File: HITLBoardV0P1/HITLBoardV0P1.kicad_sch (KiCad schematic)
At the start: 4 parts, among them SW1 SW_Push

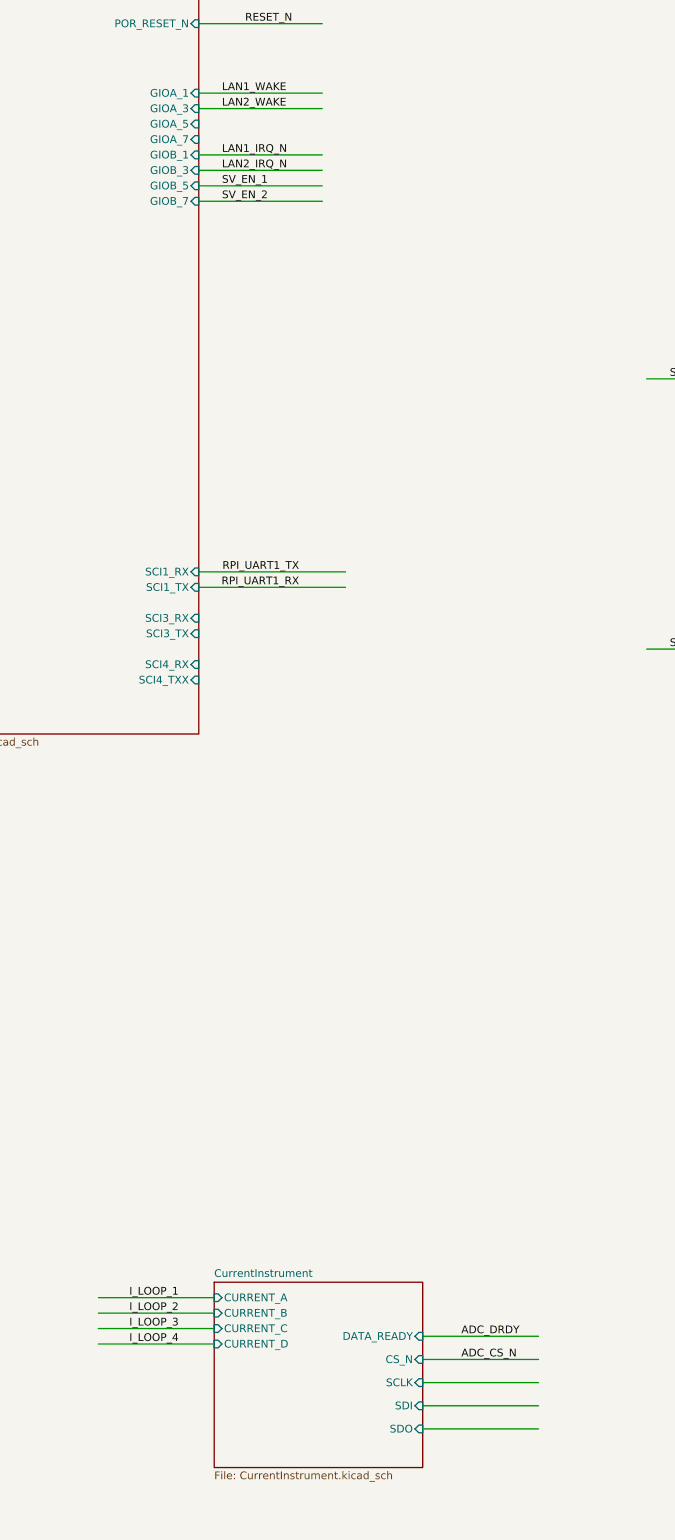
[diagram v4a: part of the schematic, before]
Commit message: FIX spi 3 on tmdx for current loop ADC, add gpio pin for data ready
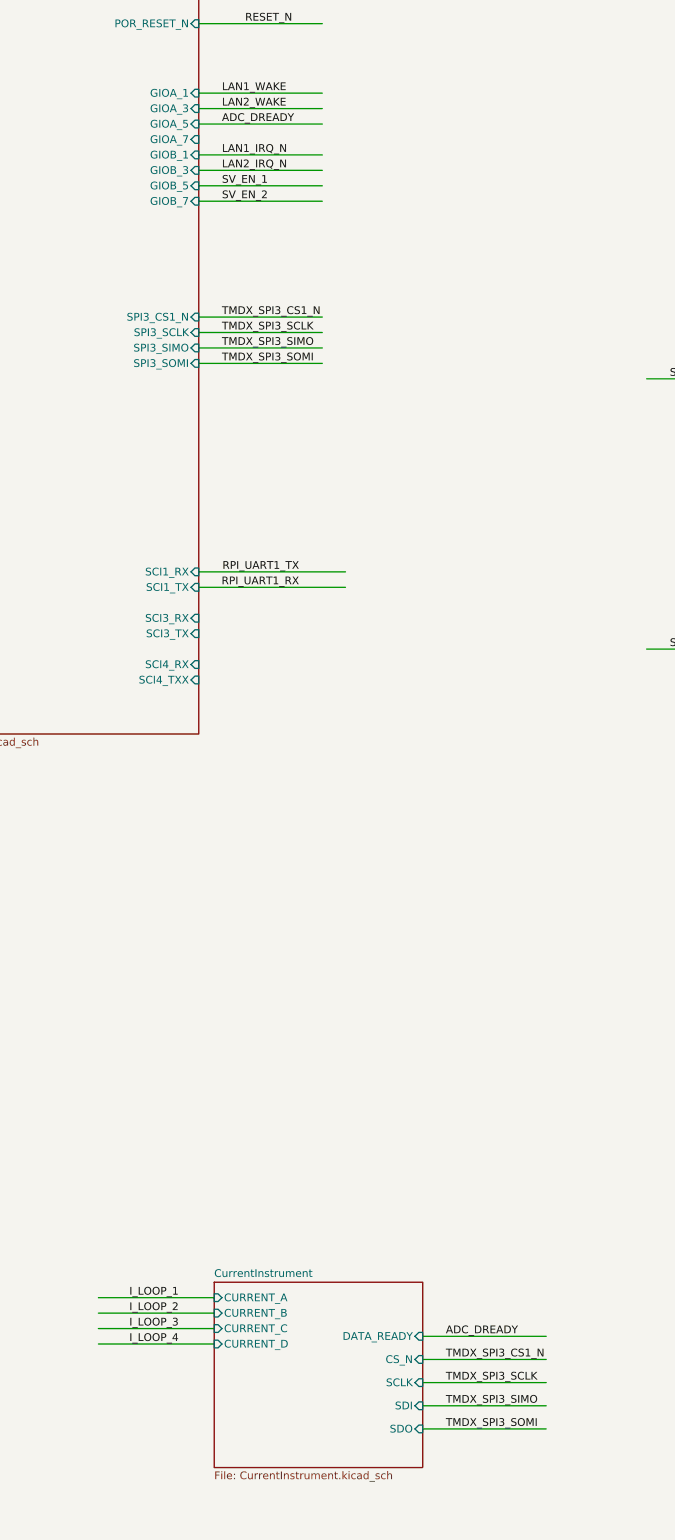
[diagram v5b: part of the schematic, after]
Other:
- sheet TMDX_Breakout ports: added SPI3_CS1_N, SPI3_SCLK, SPI3_SIMO, SPI3_SOMI; removed none
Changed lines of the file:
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@@
 	(wire
 		(pts
+			(xy 130.81 326.39) (xy 151.13 326.39)
+		)
+		(stroke
+			(width 0)
+			(type default)
+		)
+	)
+	(wire
+		(pts
 			(xy 461.01 304.8) (xy 461.01 328.93)
 		)
@@
 	(wire
 		(pts
-			(xy 130.81 334.01) (xy 149.86 334.01)
+			(xy 387.35 53.34) (xy 406.4 53.34)
 		)
 		(stroke
@@
 	(wire
 		(pts
-			(xy 387.35 53.34) (xy 406.4 53.34)
+			(xy 93.98 130.81) (xy 114.3 130.81)
 		)
 		(stroke
@@
 	(wire
 		(pts
-			(xy 93.98 130.81) (xy 114.3 130.81)
+			(xy 130.81 334.01) (xy 151.13 334.01)
 		)
 		(stroke
@@
 	(wire
 		(pts
-			(xy 290.83 314.96) (xy 314.96 314.96)
+			(xy 93.98 154.94) (xy 114.3 154.94)
 		)
 		(stroke
@@
 	(wire
 		(pts
-			(xy 130.81 326.39) (xy 149.86 326.39)
+			(xy 290.83 314.96) (xy 314.96 314.96)
 		)
 		(stroke
@@
 	(wire
 		(pts
-			(xy 130.81 337.82) (xy 149.86 337.82)
-		)
-		(stroke
-			(width 0)
-			(type default)
-		)
-	)
-	(wire
-		(pts
 			(xy 453.39 304.8) (xy 453.39 328.93)
 		)
@@
 	(wire
 		(pts
-			(xy 130.81 322.58) (xy 149.86 322.58)
-		)
-		(stroke
-			(width 0)
-			(type default)
-		)
-	)
-	(wire
-		(pts
 			(xy 457.2 304.8) (xy 457.2 328.93)
 		)
@@
 	(wire
 		(pts
+			(xy 130.81 330.2) (xy 151.13 330.2)
+		)
+		(stroke
+			(width 0)
+			(type default)
+		)
+	)
+	(wire
+		(pts
 			(xy 513.08 220.98) (xy 537.21 220.98)
 		)
@@
 	(wire
 		(pts
+			(xy 93.98 123.19) (xy 114.3 123.19)
+		)
+		(stroke
+			(width 0)
+			(type default)
+		)
+	)
+	(wire
+		(pts
+			(xy 93.98 160.02) (xy 114.3 160.02)
+		)
+		(stroke
+			(width 0)
+			(type default)
+		)
+	)
+	(wire
+		(pts
 			(xy 449.58 304.8) (xy 449.58 328.93)
 		)
@@
 	(wire
 		(pts
+			(xy 130.81 322.58) (xy 151.13 322.58)
+		)
+		(stroke
+			(width 0)
+			(type default)
+		)
+	)
+	(wire
+		(pts
 			(xy 262.89 337.82) (xy 281.94 337.82)
 		)
@@
 	(wire
 		(pts
-			(xy 130.81 330.2) (xy 149.86 330.2)
+			(xy 422.91 304.8) (xy 422.91 328.93)
 		)
 		(stroke
@@
 	(wire
 		(pts
-			(xy 422.91 304.8) (xy 422.91 328.93)
+			(xy 407.67 304.8) (xy 407.67 328.93)
 		)
 		(stroke
@@
 	(wire
 		(pts
-			(xy 407.67 304.8) (xy 407.67 328.93)
+			(xy 93.98 162.56) (xy 114.3 162.56)
 		)
 		(stroke
@@
 	(wire
 		(pts
+			(xy 93.98 157.48) (xy 114.3 157.48)
+		)
+		(stroke
+			(width 0)
+			(type default)
+		)
+	)
+	(wire
+		(pts
 			(xy 403.86 328.93) (xy 403.86 317.5)
 		)
@@
 	(wire
 		(pts
+			(xy 130.81 337.82) (xy 151.13 337.82)
+		)
+		(stroke
+			(width 0)
+			(type default)
+		)
+	)
+	(wire
+		(pts
 			(xy 93.98 196.85) (xy 118.11 196.85)
 		)
@@
 		)
 	)
+	(label "TMDX_SPI3_SOMI"
+		(at 134.62 337.82 0)
+		(effects
+			(font
+				(size 1.27 1.27)
+			)
+			(justify left bottom)
+		)
+	)
 	(label "TMDX_SPI5_SIMO"
 		(at 97.79 82.55 0)
@@
 		)
 	)
-	(label "ADC_DRDY"
-		(at 137.16 322.58 0)
-		(effects
-			(font
-				(size 1.27 1.27)
-			)
-			(justify left bottom)
-		)
-	)
 	(label "RPI_I2C_SCL"
 		(at 491.49 325.12 90)
@@
 		)
 	)
+	(label "TMDX_SPI3_SOMI"
+		(at 97.79 162.56 0)
+		(effects
+			(font
+				(size 1.27 1.27)
+			)
+			(justify left bottom)
+		)
+	)
 	(label "LAN1_WAKE"
 		(at 307.34 74.93 0)
@@
 		)
 	)
+	(label "TMDX_SPI3_SCLK"
+		(at 134.62 330.2 0)
+		(effects
+			(font
+				(size 1.27 1.27)
+			)
+			(justify left bottom)
+		)
+	)
 	(label "DAC_CLR1"
 		(at 228.6 332.74 180)
@@
 		)
 	)
+	(label "ADC_DREADY"
+		(at 97.79 123.19 0)
+		(effects
+			(font
+				(size 1.27 1.27)
+			)
+			(justify left bottom)
+		)
+	)
 	(label "LAN_RESET_N_0"
 		(at 464.82 321.31 90)
@@
 		)
 	)
+	(label "TMDX_SPI3_SIMO"
+		(at 134.62 334.01 0)
+		(effects
+			(font
+				(size 1.27 1.27)
+			)
+			(justify left bottom)
+		)
+	)
 	(label "TMDX_SPI1_CS1"
 		(at 99.06 67.31 0)
@@
 		)
 	)
+	(label "TMDX_SPI3_CS1_N"
+		(at 134.62 326.39 0)
+		(effects
+			(font
+				(size 1.27 1.27)
+			)
+			(justify left bottom)
+		)
+	)
 	(label "SV_ON_2"
 		(at 232.41 209.55 0)
@@
 		)
 	)
+	(label "ADC_DREADY"
+		(at 134.62 322.58 0)
+		(effects
+			(font
+				(size 1.27 1.27)
+			)
+			(justify left bottom)
+		)
+	)
 	(label "RPI_SPI1_MISO"
 		(at 294.64 347.98 0)
@@
 		)
 	)
+	(label "TMDX_SPI3_CS1_N"
+		(at 97.79 154.94 0)
+		(effects
+			(font
+				(size 1.27 1.27)
+			)
+			(justify left bottom)
+		)
+	)
 	(label "RPI_SPI0_MISO"
 		(at 450.85 138.43 180)
@@
 		)
 	)
-	(label "I_LOOP_3"
-		(at 346.71 306.07 0)
+	(label "TMDX_SPI3_SIMO"
+		(at 97.79 160.02 0)
 		(effects
 			(font
@@
 		)
 	)
-	(label "SPI0_CS0"
-		(at 450.85 127 180)
+	(label "I_LOOP_3"
+		(at 346.71 306.07 0)
 		(effects
 			(font
 				(size 1.27 1.27)
 			)
-			(justify right bottom)
+			(justify left bottom)
 		)
 	)
-	(label "ADC_CS_N"
-		(at 137.16 326.39 0)
+	(label "SPI0_CS0"
+		(at 450.85 127 180)
 		(effects
 			(font
 				(size 1.27 1.27)
 			)
-			(justify left bottom)
+			(justify right bottom)
 		)
 	)
@@
 		)
 	)
+	(label "TMDX_SPI3_SCLK"
+		(at 97.79 157.48 0)
+		(effects
+			(font
+				(size 1.27 1.27)
+			)
+			(justify left bottom)
+		)
+	)
 	(label "TMDX_SPI5_SIMO"
 		(at 306.07 133.35 0)
@@
 			(effects
 				(font
+					(size 1.27 1.27)
+				)
+				(justify right)
+			)
+		)
+		(pin "SPI3_CS1_N" input
+			(at 93.98 154.94 0)
+			(effects
+				(font
+					(size 1.27 1.27)
+				)
+				(justify right)
+			)
+		)
+		(pin "SPI3_SCLK" input
+			(at 93.98 157.48 0)
+			(effects
+				(font
+					(size 1.27 1.27)
+				)
+				(justify right)
+			)
+		)
+		(pin "SPI3_SIMO" input
+			(at 93.98 160.02 0)
+			(effects
+				(font
+					(size 1.27 1.27)
+				)
+				(justify right)
+			)
+		)
+		(pin "SPI3_SOMI" input
+			(at 93.98 162.56 0)
+			(effects
+				(font

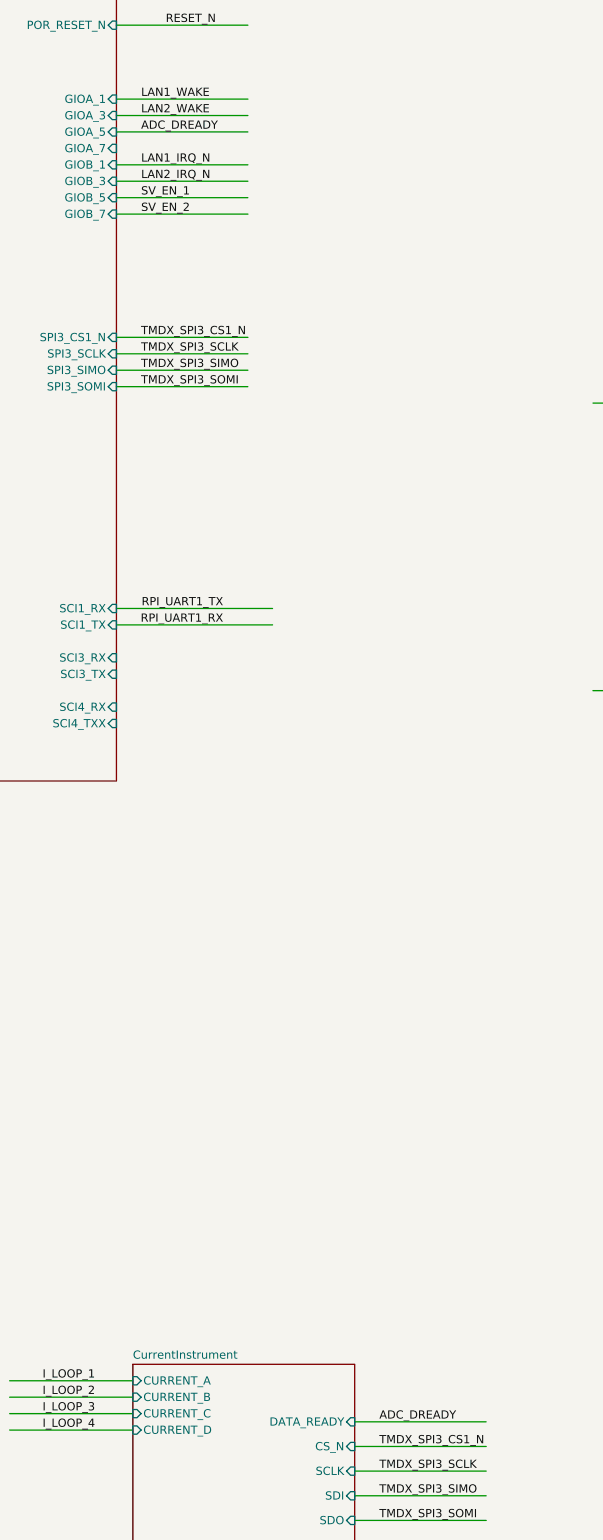
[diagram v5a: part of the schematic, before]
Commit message: basic organization into layout
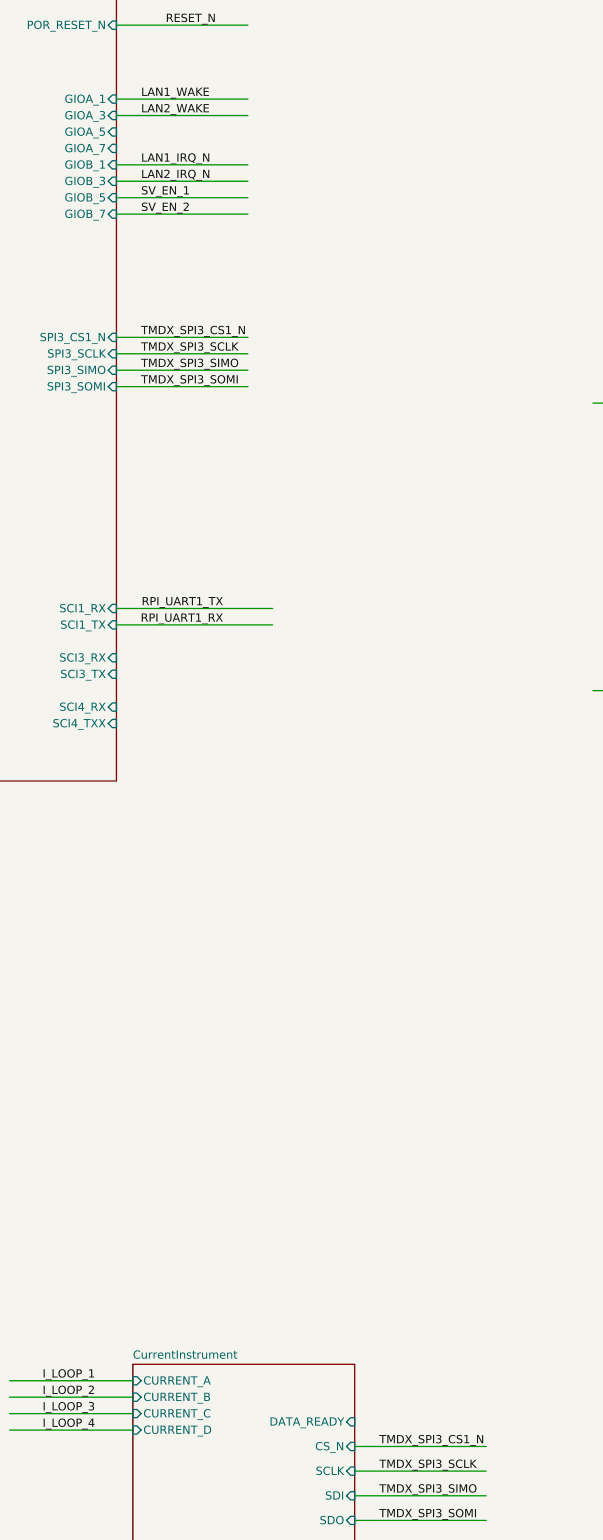
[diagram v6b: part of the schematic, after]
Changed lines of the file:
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@@
-	(wire
-		(pts
-			(xy 93.98 123.19) (xy 114.3 123.19)
-		)
-		(stroke
-			(width 0)
-			(type default)
-		)
-	)
 	(wire
 		(pts
@@
 		(pts
 			(xy 93.98 80.01) (xy 116.84 80.01)
-		)
-		(stroke
-			(width 0)
-			(type default)
-		)
-	)
-	(wire
-		(pts
-			(xy 130.81 322.58) (xy 151.13 322.58)
 		)
 		(stroke
@@
 		)
 	)
-	(label "ADC_DREADY"
-		(at 97.79 123.19 0)
-		(effects
-			(font
-				(size 1.27 1.27)
-			)
-			(justify left bottom)
-		)
-	)
 	(label "LAN_RESET_N_0"
 		(at 464.82 321.31 90)
@@
 		(effects
 			(font
-				(size 1.27 1.27)
-			)
-			(justify left bottom)
-		)
-	)
-	(label "ADC_DREADY"
-		(at 134.62 322.58 0)
-		(effects
-			(font
